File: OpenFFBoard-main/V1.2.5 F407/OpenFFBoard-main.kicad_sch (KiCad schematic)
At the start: 63 parts, among them J1 USB4105-GF-A, SW1 TL3342F160QG, SW2 TL3342F160QG, U1 STM32F407VGT6, U2 TJA1051T-3, U3 LM1117-3.3, U4 USBLC6-2SC6, X1 8MHz

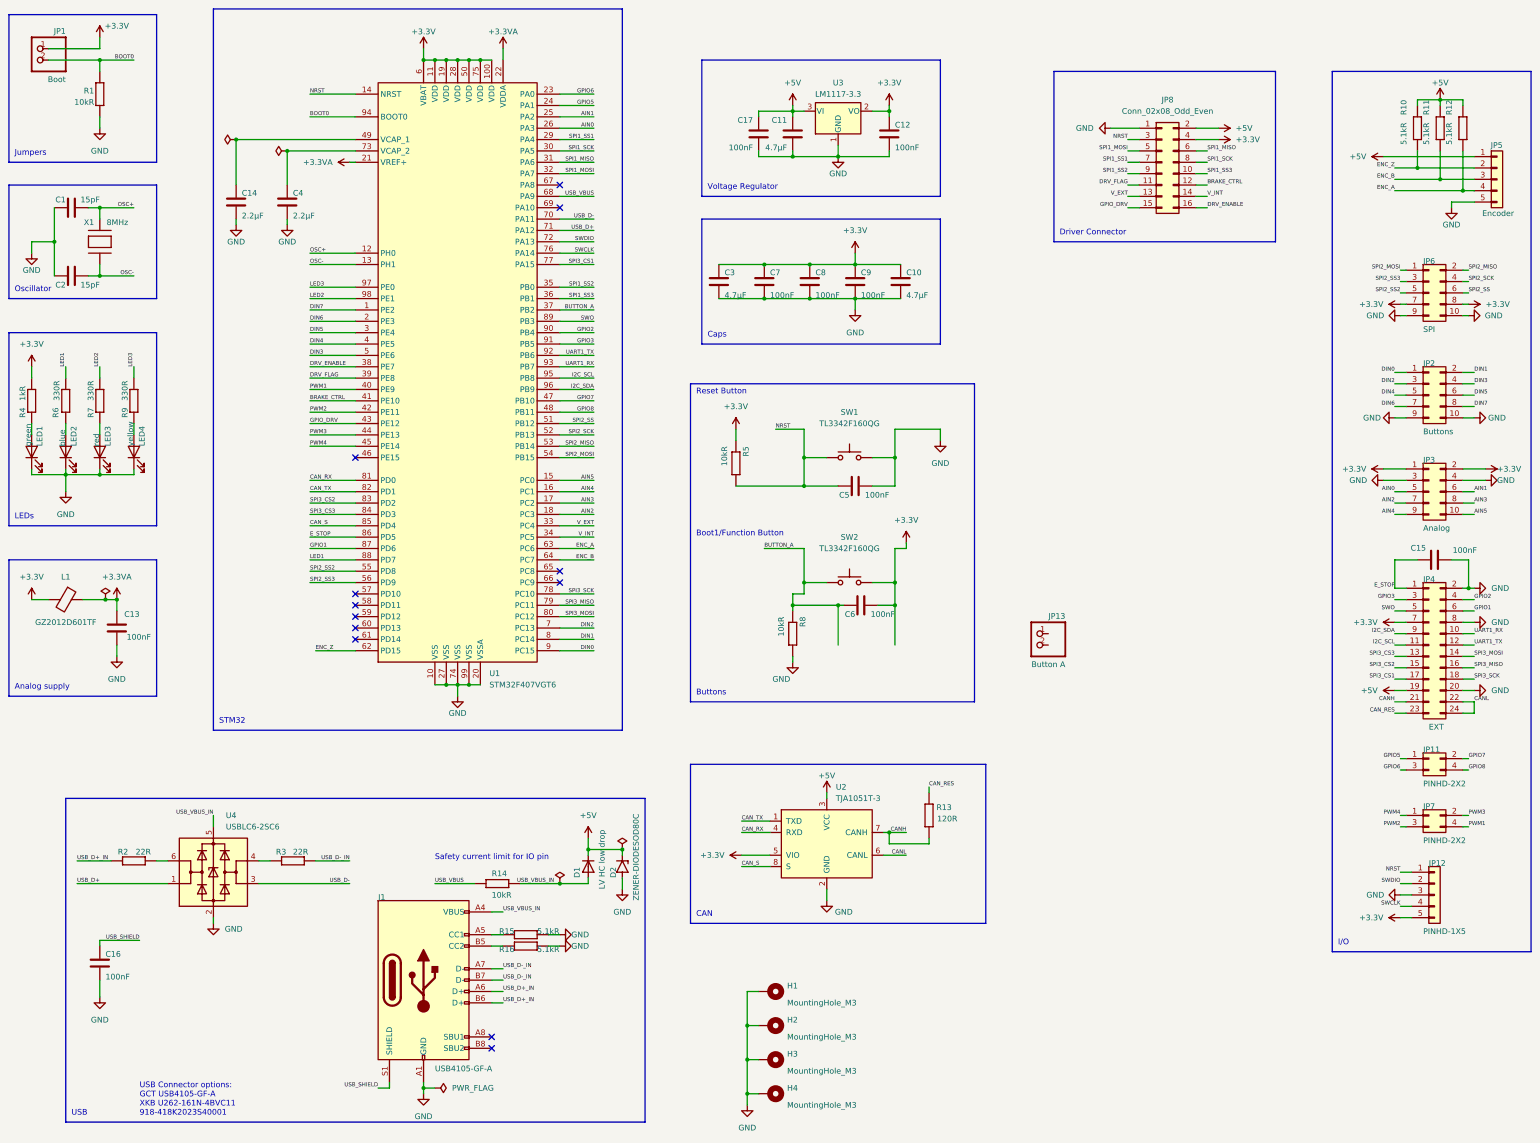
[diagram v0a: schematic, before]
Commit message: defined net class rules and added missing 3d models
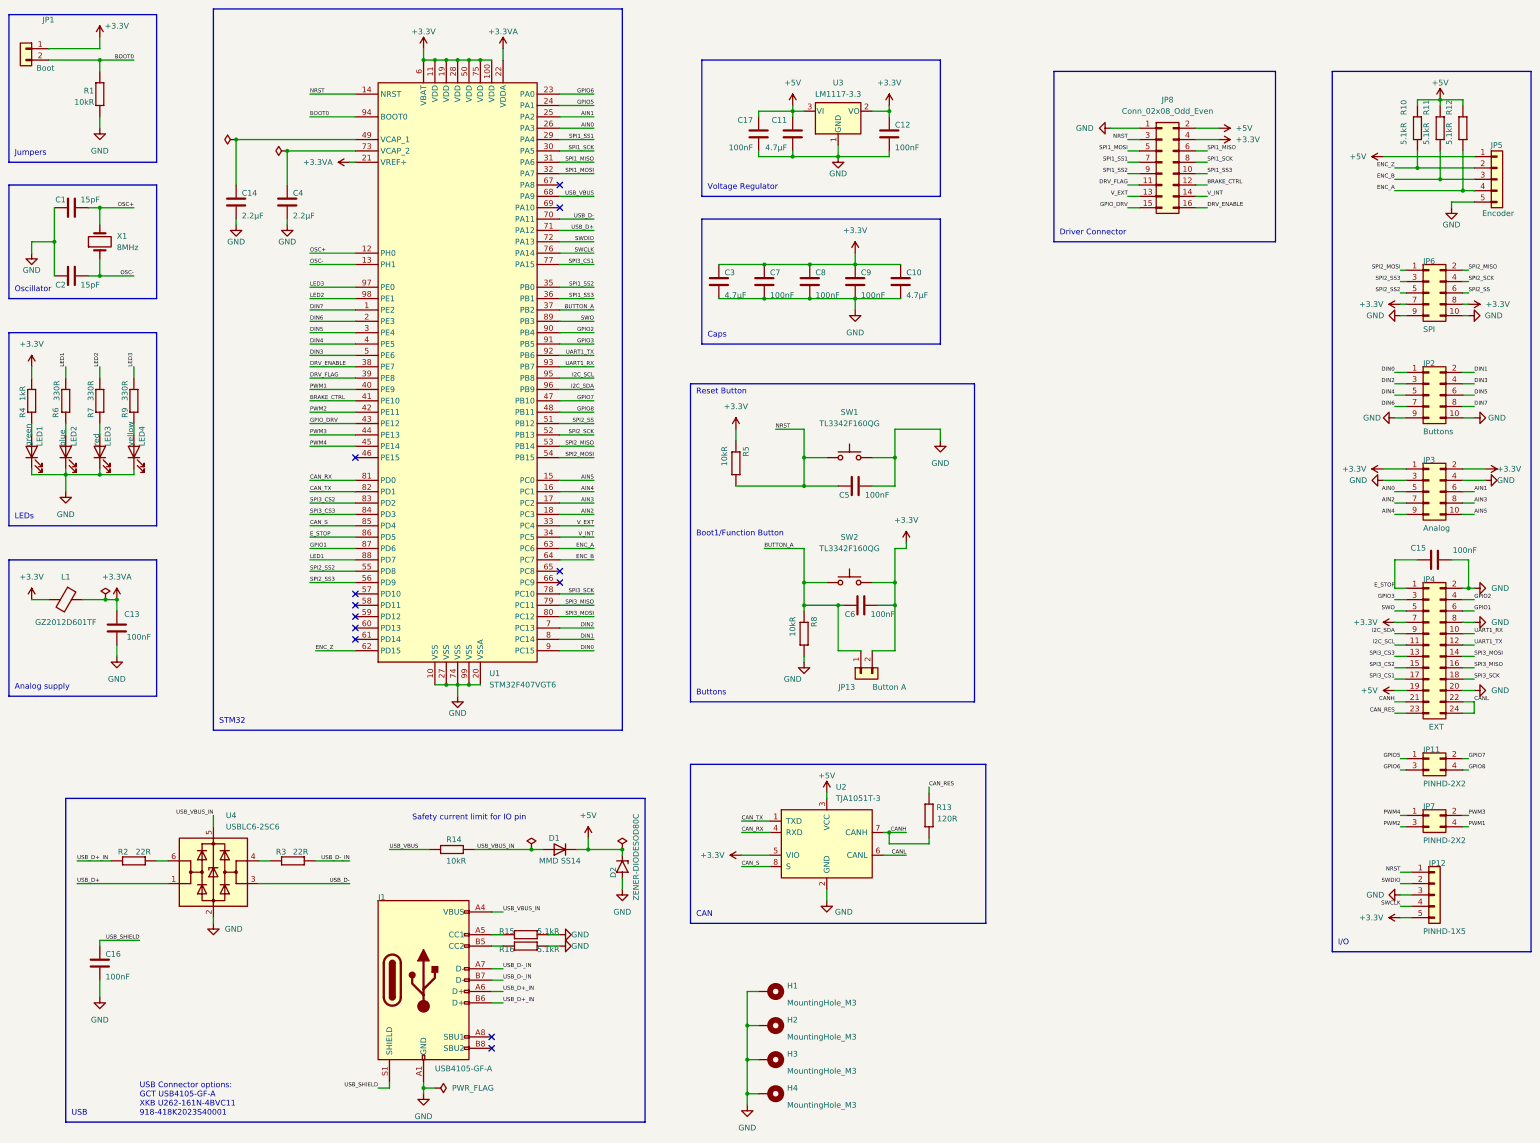
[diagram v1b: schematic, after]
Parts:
- removed D1: LV HC low drop, stm_board_f407_1.2.4:SMADIODE, symbol stm_board_f407_1.2.4-eagle-import:DIODESMA
- removed X1: 8MHz, stm_board_f407_1.2.4:NX5032, symbol stm_board_f407_1.2.4-eagle-import:XTALNX5032
- added D1: MMD SS14, Diode_SMD:D_SMA_Handsoldering, symbol Device:D
- added X1: 8MHz, Crystal:Crystal_SMD_5032-2Pin_5.0x3.2mm, symbol Device:Crystal
- J1: footprint stm_board_f407_1.2.4:GCT_USB4105-GF-A -> Connector_USB:USB_C_Receptacle_Palconn_UTC16-G
- JP1, JP13: footprint stm_board_f407_1.2.4:1X02 -> Connector_PinHeader_2.54mm:PinHeader_1x02_P2.54mm_Vertical; symbol stm_board_f407_1.2.4-eagle-import:PINHD-1X2 -> Connector_Generic:Conn_01x02
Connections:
- net +3.3V: now also JP13.2 (Pin_2)
- net +5V: now also D1.1 (K)
- net BUTTON_A: now also JP13.1 (Pin_1)
- net OSC+: now also X1.2
- net OSC-: now also X1.1
- net USB_VBUS_IN: now also D1.2 (A)
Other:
- moved on the sheet: R14, R8
